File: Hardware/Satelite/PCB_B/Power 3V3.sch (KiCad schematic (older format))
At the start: 17 parts, among them U2 ADP2108AUJ-3.3, U3 INA194, U4 MCP6001-OT

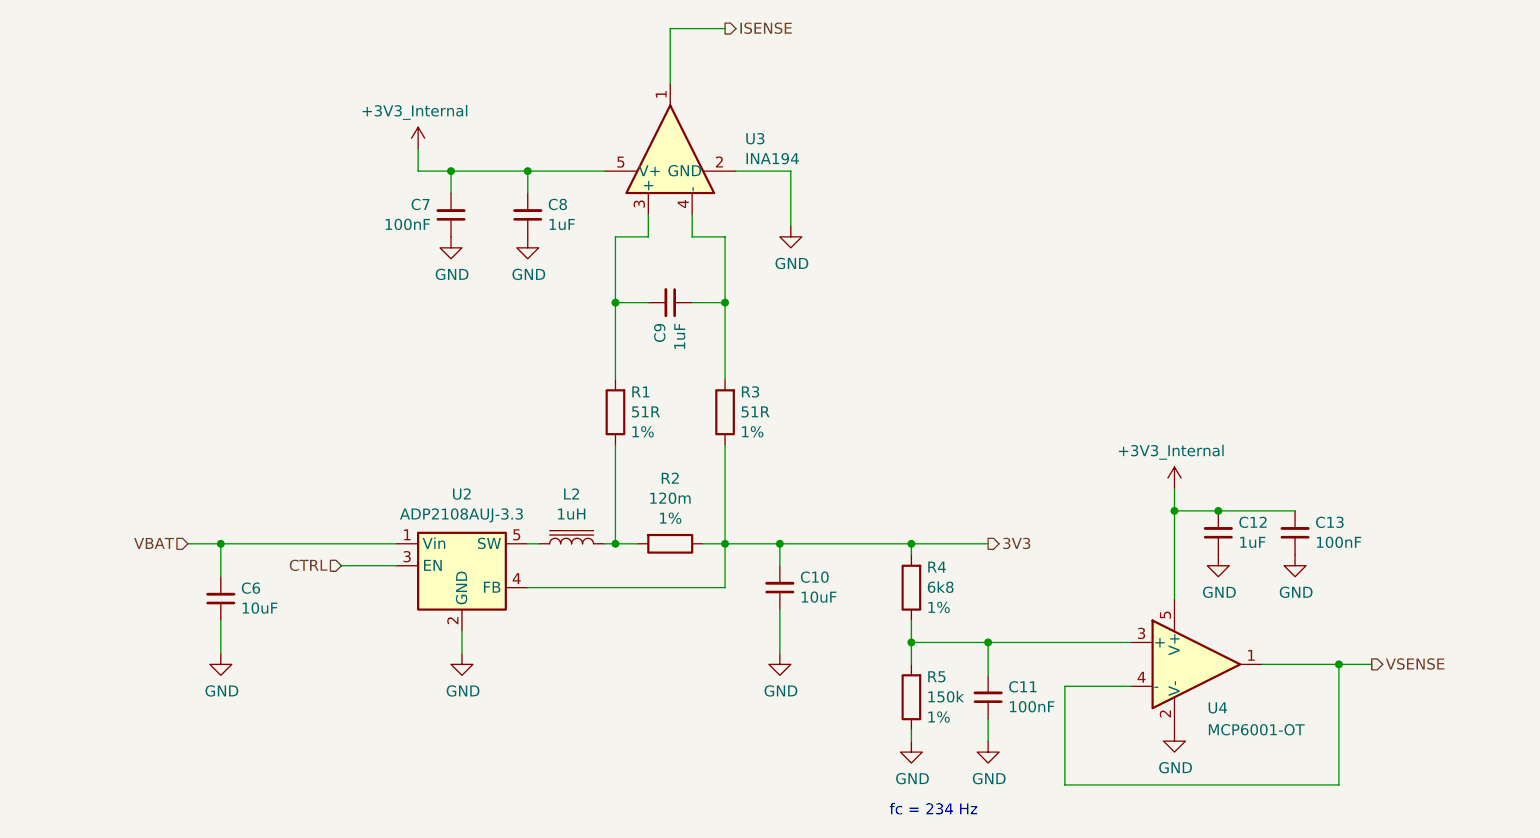
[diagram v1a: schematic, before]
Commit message: Agregado de MOSFET para cortar las fuentes de 3.3V y 5V en el PCB_B en lugar de usar los enable
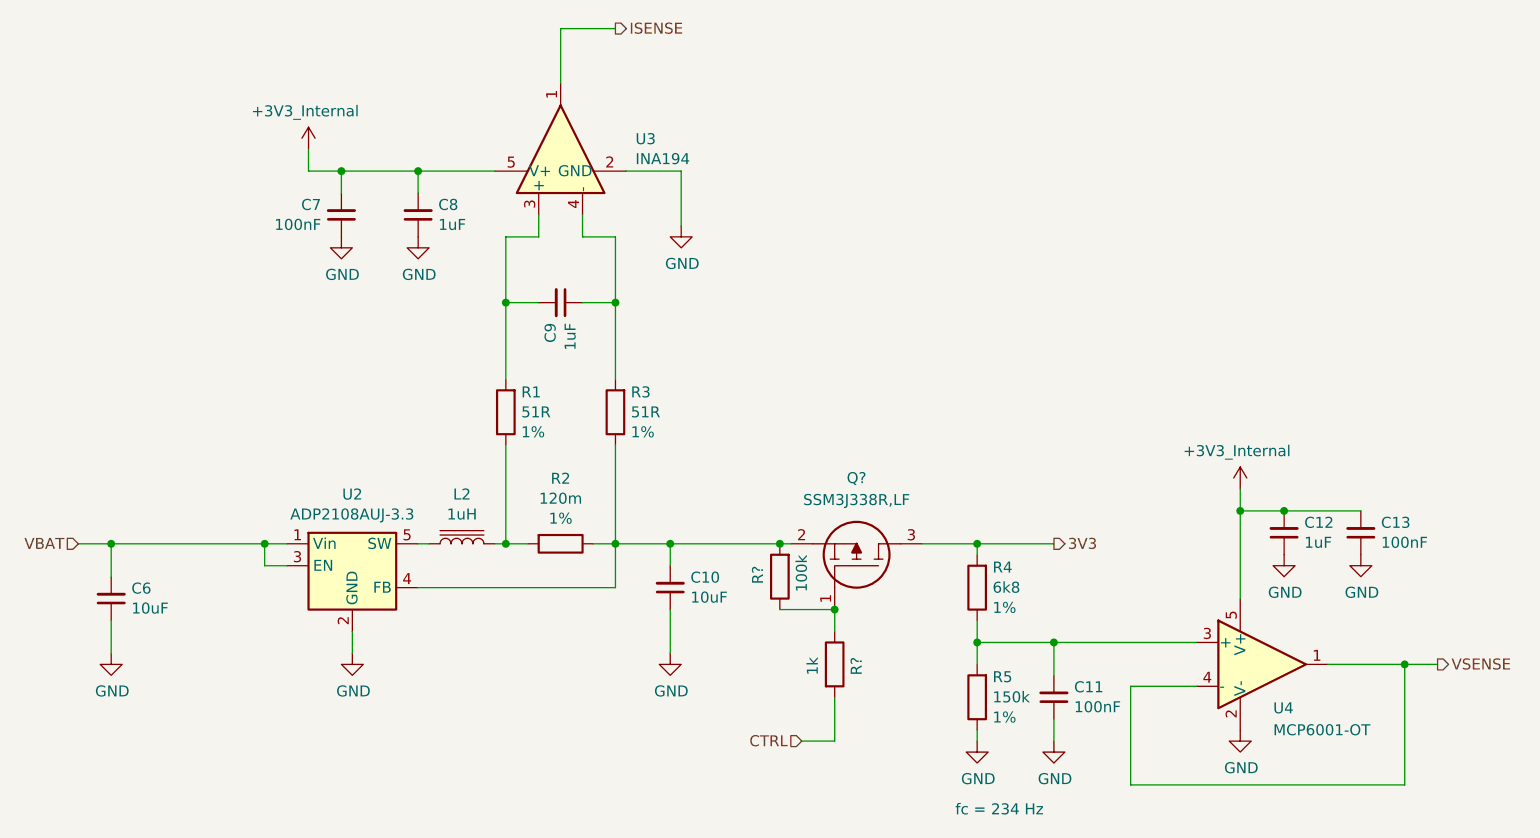
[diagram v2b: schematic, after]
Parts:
- added Q?: SSM3J338R,LF, SamacSys_Parts:SSM3J332RLFT, symbol SamacSys_Parts:SSM3J338R,LF
- added R?: 100k, Resistor_SMD:R_0603_1608Metric_Pad1.05x0.95mm_HandSolder, symbol Device:R
- added R?: 1k, Capacitor_SMD:C_0603_1608Metric_Pad1.05x0.95mm_HandSolder, symbol Device:R
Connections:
- net 3V3: now also Q?.3; no longer C10.2, R2.1, R3.1, U2.4 (FB)
- net CTRL: now also R?.2; no longer U2.3 (EN)
- net VBAT: now also U2.3 (EN)
- new net: C10.2, Q?.2, R2.1, R3.1, R?.2, U2.4 (FB)
- new net: Q?.1, R?.1, R?.1
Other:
- moved on the sheet: C10, C11, C12, C13, C6, C7, C8, C9, L2, R1, R2, R3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

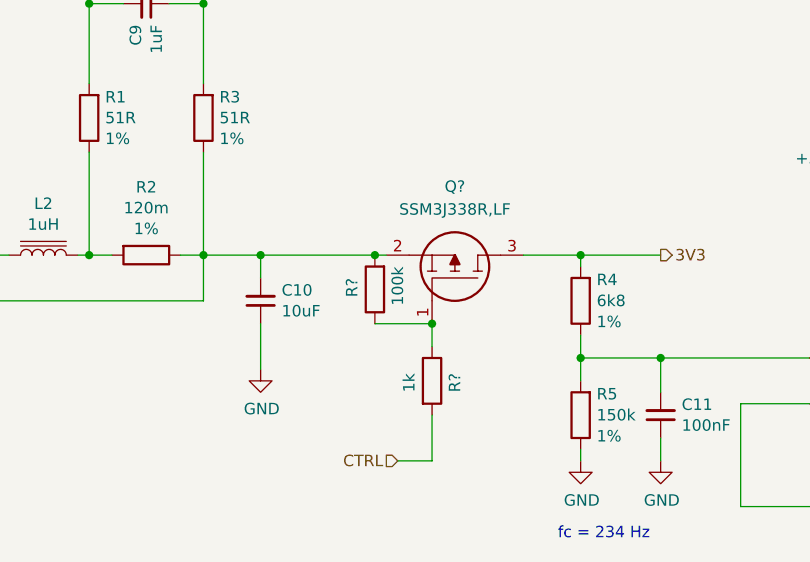
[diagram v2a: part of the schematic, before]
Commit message: Nuevo LDO de más corriente para 3.3V internos en PCB_B
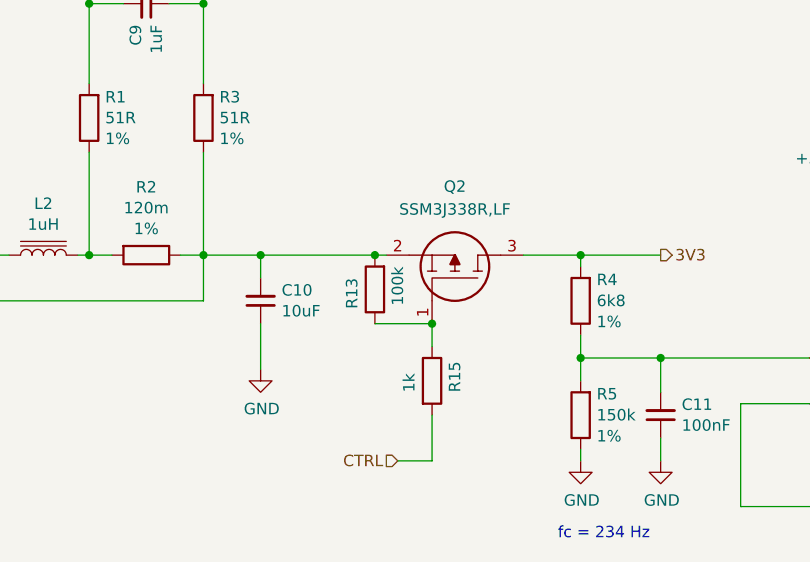
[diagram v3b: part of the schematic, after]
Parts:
- gave numbers to parts that had none: 3
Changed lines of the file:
@@
 AR Path="/5D24EEFF" Ref="Q?"  Part="1"
 AR Path="/5BC14C3C/5D24EEFF" Ref="Q?"  Part="1"
-AR Path="/5BC13C37/5D24EEFF" Ref="Q?"  Part="1"
-F 0 "Q?" V 6950 4700 50  0000 C CNN
+AR Path="/5BC13C37/5D24EEFF" Ref="Q2"  Part="1"
+F 0 "Q2" V 6950 4700 50  0000 C CNN
 F 1 "SSM3J338R,LF" V 6850 4700 50  0000 C CNN
 F 2 "SamacSys_Parts:SSM3J332RLFT" H 6800 4550 50  0001 L CNN
@@
 AR Path="/5BC300BF/5D24EF0A" Ref="R?"  Part="1"
 AR Path="/5BC14C3C/5D24EF0A" Ref="R?"  Part="1"
-AR Path="/5BC13C37/5D24EF0A" Ref="R?"  Part="1"
-F 0 "R?" V 6200 4400 50  0000 L CNN
+AR Path="/5BC13C37/5D24EF0A" Ref="R13"  Part="1"
+F 0 "R13" V 6200 4400 50  0000 L CNN
 F 1 "100k" V 6000 4350 50  0000 L CNN
 F 2 "Resistor_SMD:R_0603_1608Metric_Pad1.05x0.95mm_HandSolder" V 6030 4450 50  0001 C CNN
@@
 AR Path="/5BB1631B/5D24EF13" Ref="R?"  Part="1"
 AR Path="/5BC28DAC/5D24EF13" Ref="R?"  Part="1"
-AR Path="/5BC13C37/5D24EF13" Ref="R?"  Part="1"
-F 0 "R?" V 6450 4800 50  0000 L CNN
+AR Path="/5BC13C37/5D24EF13" Ref="R15"  Part="1"
+F 0 "R15" V 6450 4800 50  0000 L CNN
 F 1 "1k" V 6250 4800 50  0000 L CNN
 F 2 "Capacitor_SMD:C_0603_1608Metric_Pad1.05x0.95mm_HandSolder" V 6280 4850 50  0001 C CNN
